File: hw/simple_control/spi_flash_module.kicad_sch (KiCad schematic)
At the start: 2 parts, among them J7 Conn_01x06

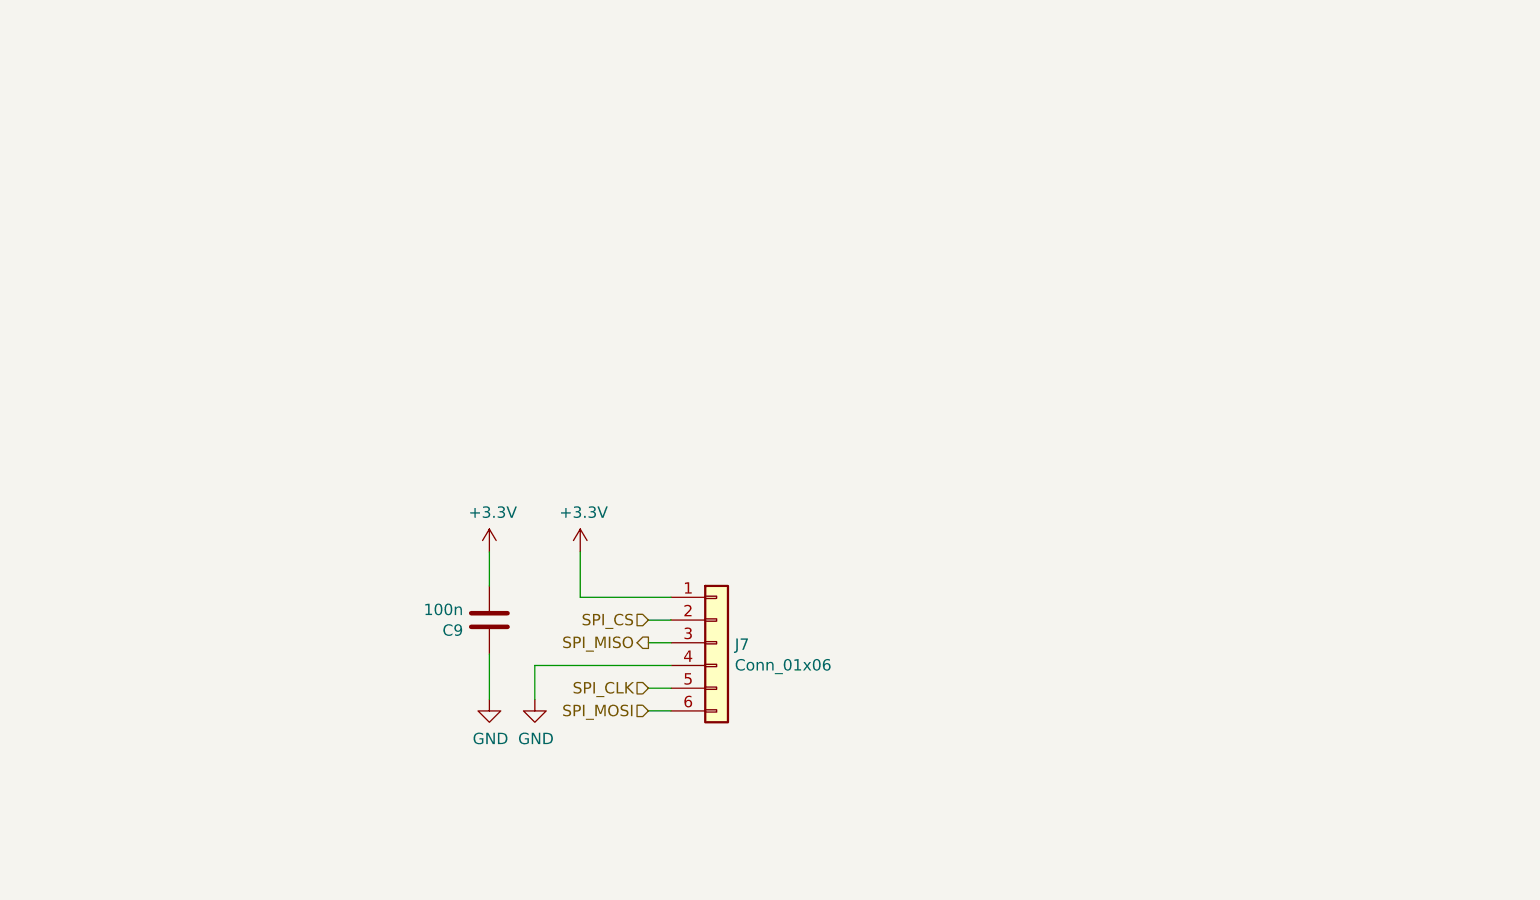
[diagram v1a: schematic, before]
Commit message: chore(hw): swap SPI flash module for SD card
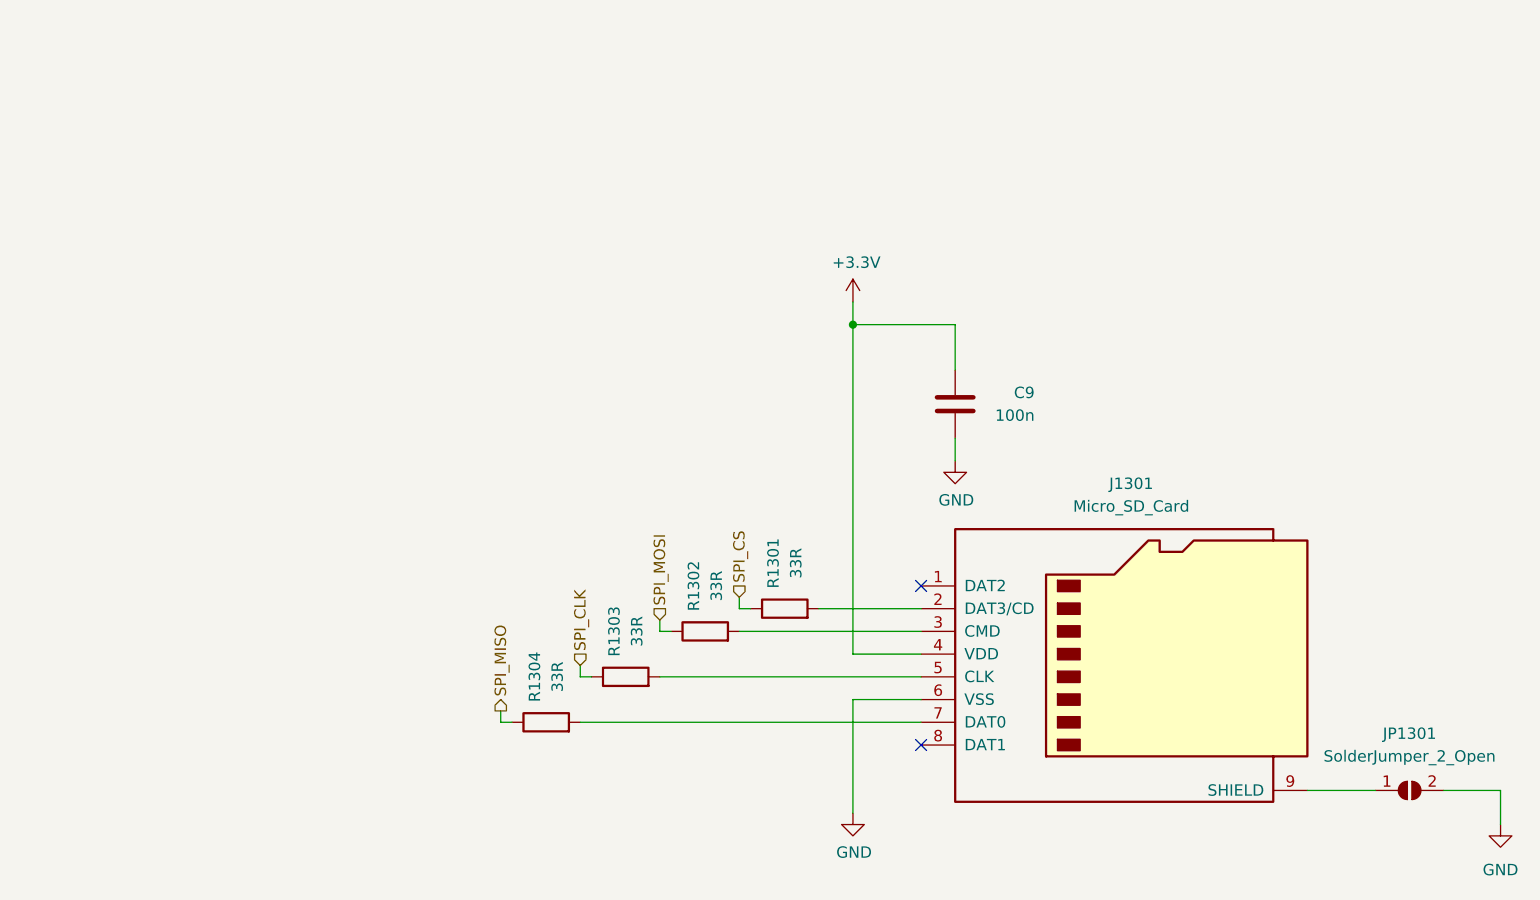
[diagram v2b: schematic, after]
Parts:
- removed J7: Conn_01x06, Connector_PinSocket_2.54mm:PinSocket_1x06_P2.54mm_Vertical, symbol Connector_Generic:Conn_01x06
- added J1301: Micro_SD_Card, my:micro_sd_card, symbol Connector:Micro_SD_Card
- added JP1301: SolderJumper_2_Open, Jumper:SolderJumper-2_P1.3mm_Open_RoundedPad1.0x1.5mm, symbol Jumper:SolderJumper_2_Open
- added R1301, R1302, R1303, R1304: 33R, Resistor_SMD:R_0805_2012Metric_Pad1.20x1.40mm_HandSolder, symbol Device:R
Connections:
- net +3.3V: now also J1301.4 (VDD)
- net GND: now also J1301.6 (VSS), JP1301.2 (B)
- net SPI_CLK: now also R1303.1
- net SPI_CS: now also R1301.1
- net SPI_MISO: now also R1304.1
- net SPI_MOSI: now also R1302.1
- new net: J1301.3 (CMD), R1302.2
- new net: J1301.2 (DAT3/CD), R1301.2
- new net: J1301.5 (CLK), R1303.2
- new net: J1301.7 (DAT0), R1304.2
- new net: J1301.9 (SHIELD), JP1301.1 (A)
- no-connect marks 0 -> 2
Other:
- moved on the sheet: C9

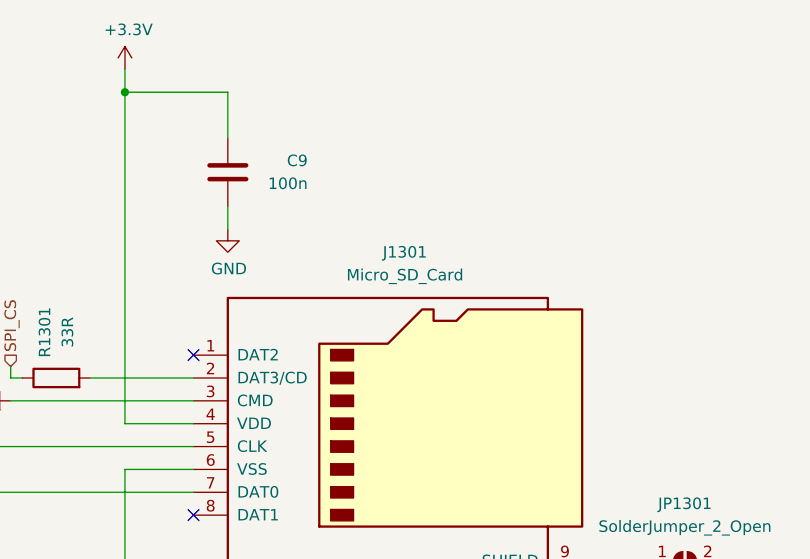
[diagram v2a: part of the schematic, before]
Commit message: chore(hw): specify SD card holder model
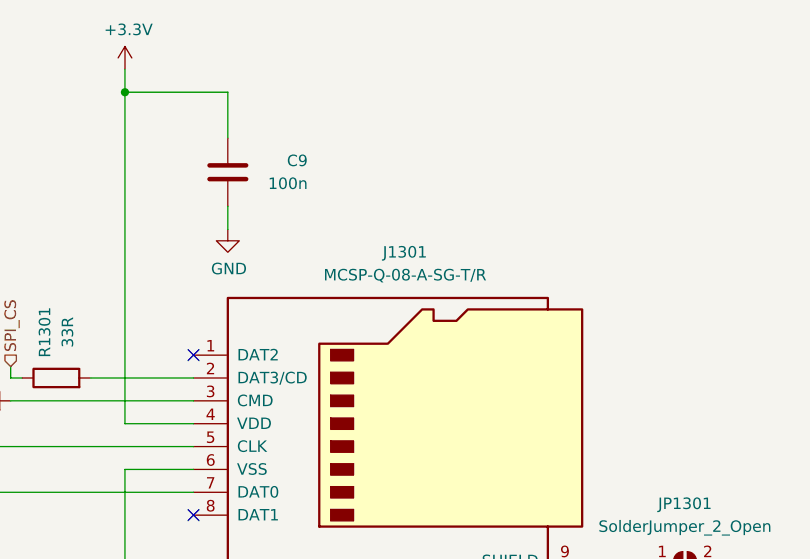
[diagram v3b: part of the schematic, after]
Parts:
- J1301: value Micro_SD_Card -> MCSP-Q-08-A-SG-T/R
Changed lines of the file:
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@@
       (effects (font (size 1.27 1.27)))
     )
-    (property "Value" "Micro_SD_Card" (at 196.215 88.9 0)
+    (property "Value" "MCSP-Q-08-A-SG-T/R" (at 196.215 88.9 0)
       (effects (font (size 1.27 1.27)))
     )

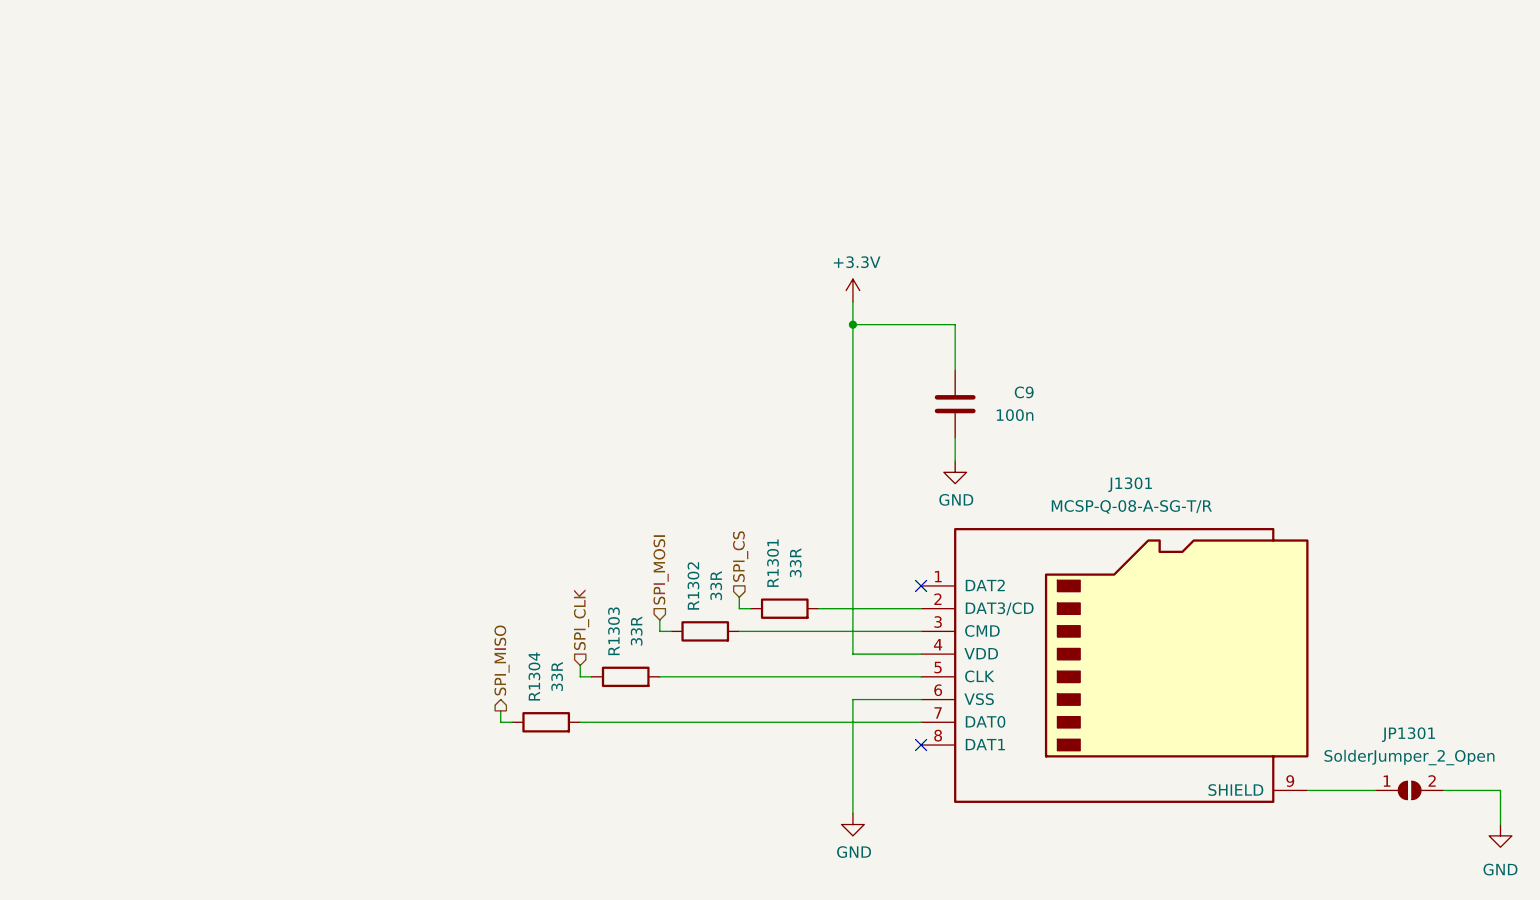
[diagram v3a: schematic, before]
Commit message: chore(hw): add dedicated 3.3V supply for SD Card
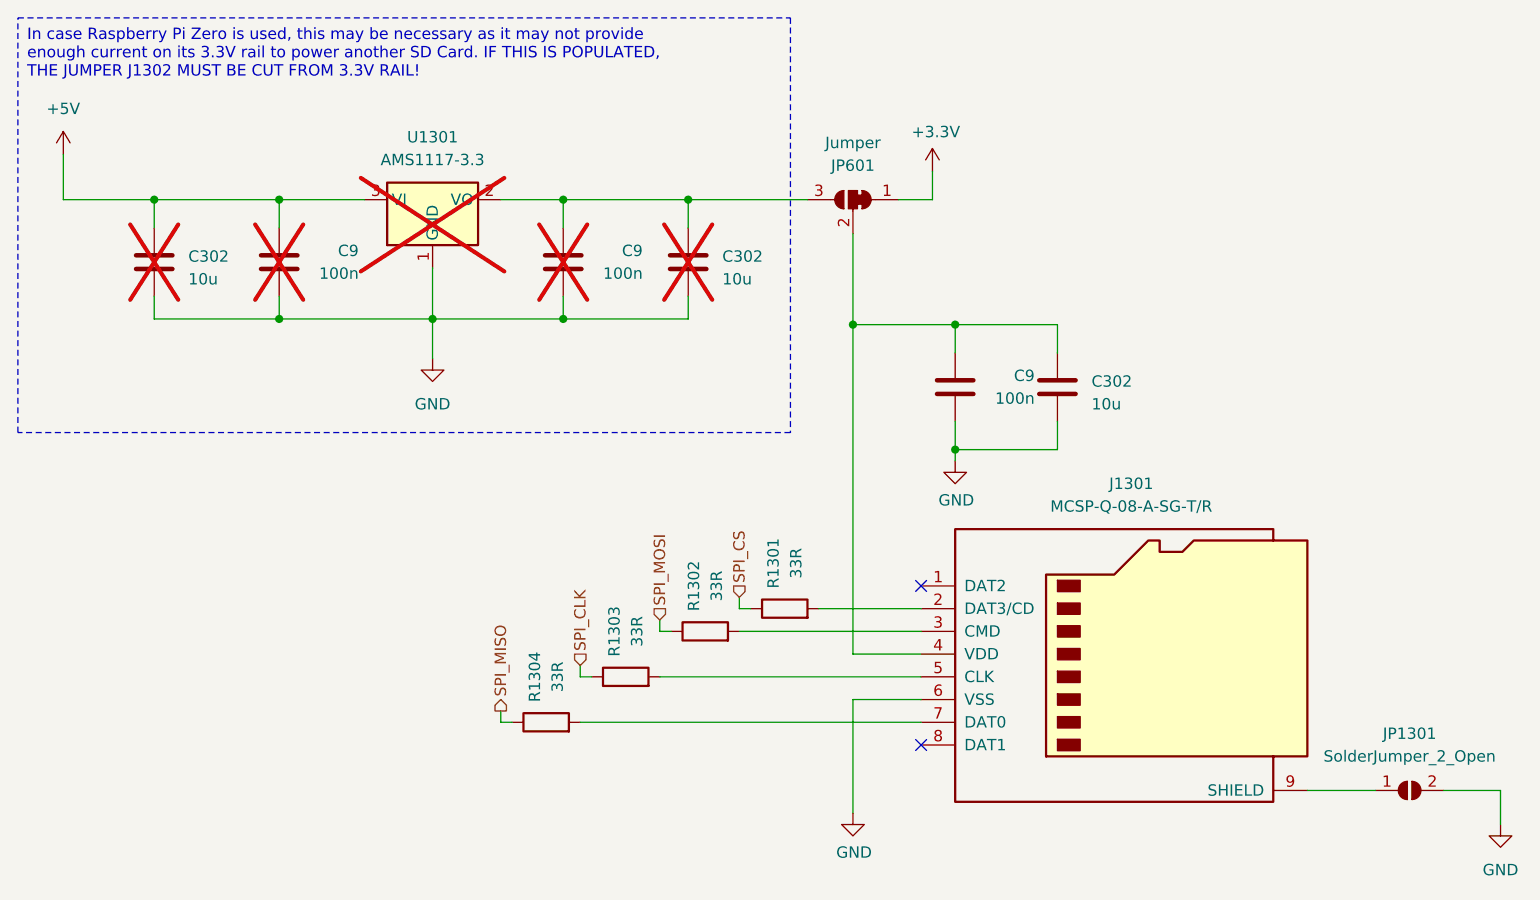
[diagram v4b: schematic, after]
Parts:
- added C302 (x3): 10u, Capacitor_SMD:C_1206_3216Metric_Pad1.33x1.80mm_HandSolder, symbol Device:C
- added C9 (x2): 100n, Capacitor_SMD:C_0805_2012Metric_Pad1.18x1.45mm_HandSolder, symbol Device:C
- added JP601: Jumper, Jumper:SolderJumper-3_P1.3mm_Bridged12_RoundedPad1.0x1.5mm_NumberLabels, symbol Jumper:SolderJumper_3_Bridged12
- added U1301: AMS1117-3.3, Package_TO_SOT_SMD:SOT-223-3_TabPin2, symbol Regulator_Linear:AMS1117-3.3
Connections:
- net +3.3V: now also JP601.1 (A); no longer C9.2, J1301.4 (VDD)
- net GND: now also C302.2, C302.2, C302.2, C9.1, C9.1, U1301.1 (GND)
- new net: C302.1, C9.2, JP601.3 (B), U1301.2 (VO)
- new net: C302.1, C9.2, J1301.4 (VDD), JP601.2 (C)
- new net +5V: C302.1, C9.2, U1301.3 (VI)
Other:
- moved on the sheet: C9
